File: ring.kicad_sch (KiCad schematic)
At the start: 29 parts, among them J1 5034800240, J2 5034800440, Q1 IRLML6344TRPBF, U1 ANNA-B112-02B, U2 LSM6DSV16X

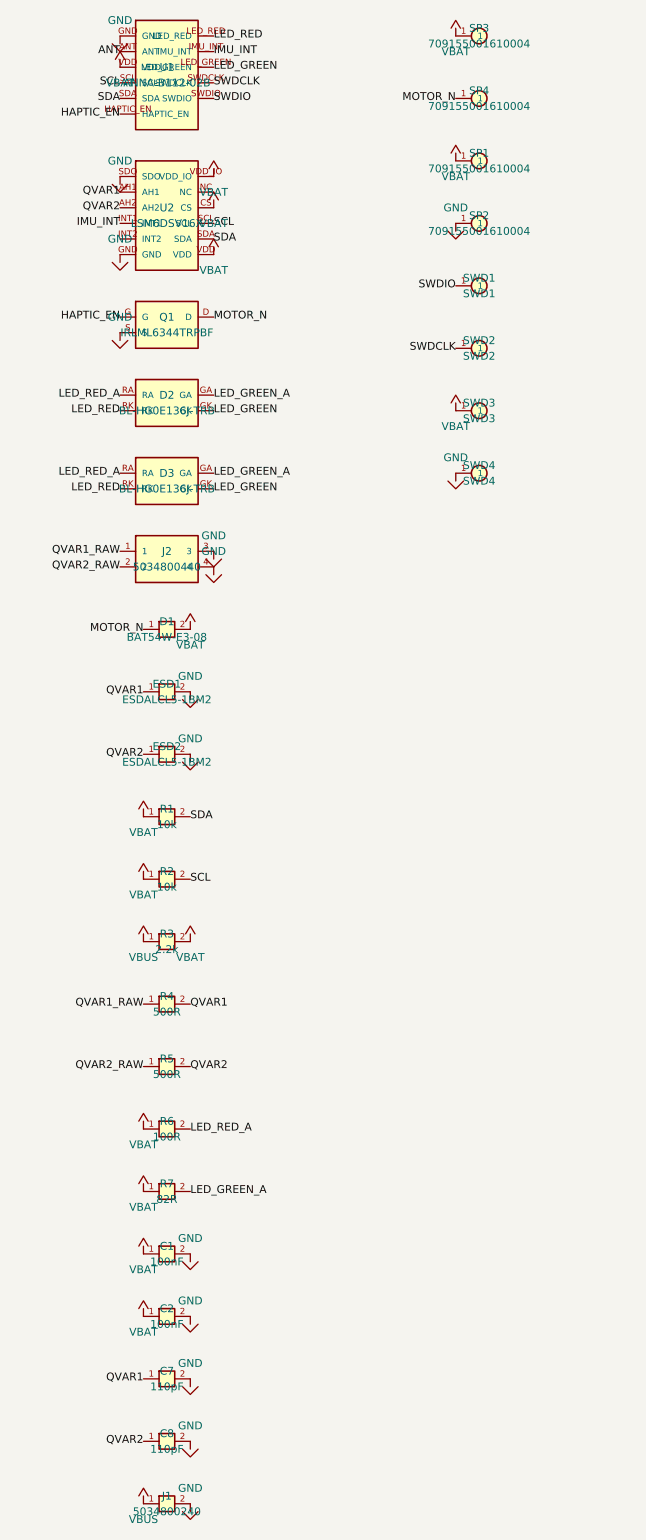
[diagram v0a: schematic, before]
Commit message: Fix bi-color LED miswire; re-solve clean (0 DRC / 0 parity)
The LEDs (D2/D3) were miswired: the net-to-pad assignment was scrambled,
so the green die had both terminals on VBAT (dead) and the red die was
GPIO-to-GPIO with no current limit. The board was DRC-clean, so it
looked fine -- but it was electrically broken, and the schematic was 111
parity-issues out of sync with the PCB.

- corrected LED net mapping (re-solved on the fixed netlist)
- schematic now matches the PCB exactly: 0 schematic-parity issues
  (symbol pin numbers = footprint pad names; global, slash-free labels)
- vias 0.4 -> 0.3mm (0.15mm drill) so the LSM6DSV16X's 0.5mm-pitch
  escapes clear the 0.127mm rule -> 0 DRC
- bom: add R8 (100k Q1 gate pull-down -- prevents uncommanded motor run
  on a floating gate at boot/reset)
- regenerated fab/ gerbers + drill, schematic PDF, board preview
- readme: honest flex-zone note (structural zoning, not a board layer)

Verified in KiCad 9: 0 DRC errors, 0 unconnected, 0 schematic-parity.

Co-Authored-By: Claude Opus 4.8 (1M context) <noreply@anthropic.com>
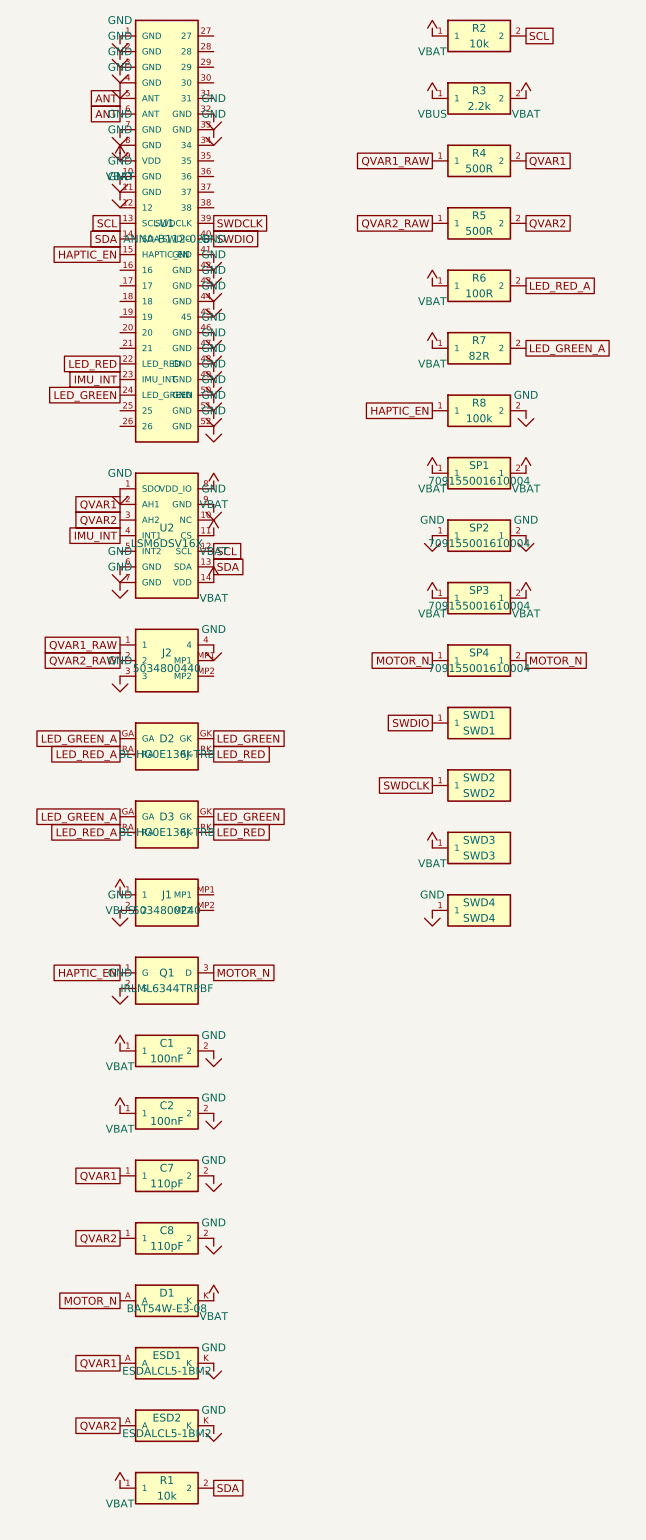
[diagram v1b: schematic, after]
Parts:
- added R8: 100k, R_0402_1005Metric, symbol ring:R8
- C1: symbol ring:C -> ring:C1
- C2: symbol ring:C -> ring:C2
- C7: footprint C_0402_1005Metric -> R_0402_1005Metric; symbol ring:C -> ring:C7
- C8: symbol ring:C -> ring:C8
- D1: symbol ring:P -> ring:D1
- ESD1: symbol ring:P -> ring:ESD1
- ESD2: symbol ring:P -> ring:ESD2
- J1: symbol ring:P -> ring:J1
- R1: symbol ring:R -> ring:R1
- R2: symbol ring:R -> ring:R2
- R3: symbol ring:R -> ring:R3
- R4: symbol ring:R -> ring:R4
- R5: symbol ring:R -> ring:R5
- R6: symbol ring:R -> ring:R6
- R7: symbol ring:R -> ring:R7
- SP1: symbol ring:Pad -> ring:SP1
- SP2: symbol ring:Pad -> ring:SP2
- SP3: symbol ring:Pad -> ring:SP3
- SP4: symbol ring:Pad -> ring:SP4
- SWD1: symbol ring:Pad -> ring:SWD1
- SWD2: symbol ring:Pad -> ring:SWD2
- SWD3: symbol ring:Pad -> ring:SWD3
- SWD4: symbol ring:Pad -> ring:SWD4
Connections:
- net ANT: now also U1.5 (ANT), U1.6 (ANT); no longer U1.ANT
- net GND: now also ESD1.K, ESD2.K, Q1.2 (S), SP2.2 (1), U1.1 (GND), U1.10 (GND), U1.11 (GND), U1.2 (GND), U1.3 (GND), U1.32 (GND), U1.33 (GND), U1.4 (GND), U1.41 (GND), U1.42 (GND), U1.43 (GND), U1.44 (GND), U1.46 (GND), U1.47 (GND), U1.48 (GND), U1.49 (GND), U1.50 (GND), U1.51 (GND), U1.52 (GND), U1.7 (GND), U1.8 (GND), U2.1 (SDO), U2.6 (GND), U2.7 (GND), U2.9 (GND), R8.2; no longer ESD1.2, ESD2.2, Q1.S, U1.GND, U2.GND, U2.SDO
- net HAPTIC_EN: now also Q1.1 (G), U1.15 (HAPTIC_EN), R8.1; no longer Q1.G, U1.HAPTIC_EN
- net IMU_INT: now also U1.23 (IMU_INT), U2.4 (INT1); no longer U1.IMU_INT, U2.INT1
- net LED_GREEN: now also U1.24 (LED_GREEN); no longer U1.LED_GREEN
- net LED_RED: now also U1.22 (LED_RED); no longer U1.LED_RED
- net MOTOR_N: now also D1.A, Q1.3 (D), SP4.2 (1); no longer D1.1, Q1.D
- net QVAR1: now also ESD1.A, U2.2 (AH1); no longer ESD1.1, U2.AH1
- net QVAR2: now also ESD2.A, U2.3 (AH2); no longer ESD2.1, U2.AH2
- net SCL: now also U1.13 (SCL), U2.12 (SCL); no longer U1.SCL, U2.SCL
- net SDA: now also U1.14 (SDA), U2.13 (SDA); no longer U1.SDA, U2.SDA
- net SWDCLK: now also U1.39 (SWDCLK); no longer U1.SWDCLK
- net SWDIO: now also U1.40 (SWDIO); no longer U1.SWDIO
- net VBAT: now also D1.K, SP1.2 (1), SP3.2 (1), U1.9 (VDD), U2.11 (CS), U2.14 (VDD), U2.8 (VDD_IO); no longer D1.2, U1.VDD, U2.CS, U2.VDD, U2.VDD_IO
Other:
- moved on the sheet: D2, D3, Q1, SWD1, SWD2, SWD3, SWD4
